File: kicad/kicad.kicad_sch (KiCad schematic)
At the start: 12 parts, among them K1 RP1A23D5, U1 WeMos_D1_mini, X1 250-202, X2 250-202, X3 250-203

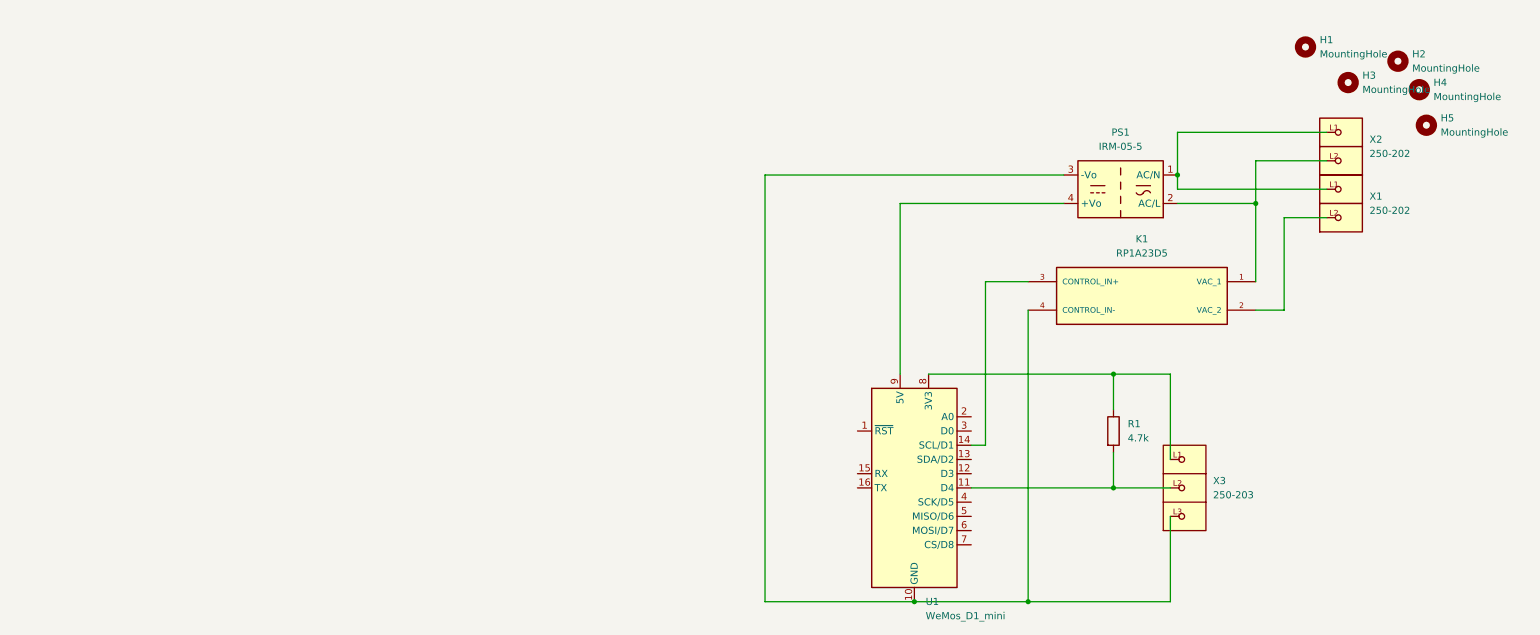
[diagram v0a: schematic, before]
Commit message: Small schematic & footprint cleanups
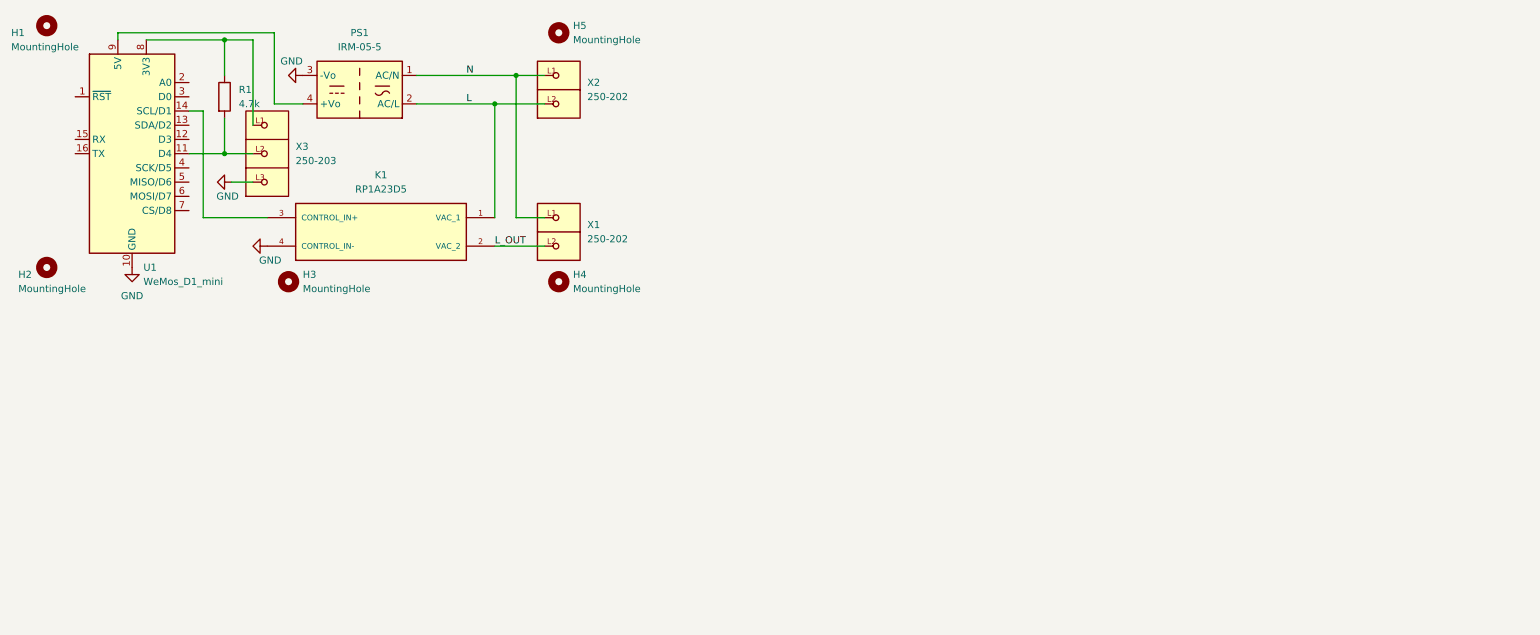
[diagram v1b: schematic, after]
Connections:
- net N: now reaches PS1.1 (AC/N), X1.L1, X2.L1
- net L: now reaches K1.1 (VAC_1), PS1.2 (AC/L), X2.L2
- net GND: now reaches K1.4 (CONTROL_IN-), PS1.3 (-Vo), U1.10 (GND), X3.L3
- net L_OUT: now reaches K1.2 (VAC_2), X1.L2
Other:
- moved on the sheet: H1, H2, H3, H4, H5, K1, PS1, R1, U1, X1, X2, X3

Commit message: WIP: some more schematic & footprint updates
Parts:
- H1, H2, H3, H4, H5: footprint MountingHole:MountingHole_2.5mm -> MountingHole:MountingHole_2.7mm_M2.5
- K1: footprint RELAY_RP1A23D5 -> snapeda-libraries:RELAY_RP1A23D5
- R1: footprint Resistor_THT:R_Axial_DIN0207_L6.3mm_D2.5mm_P7.62mm_Horizontal -> Resistor_THT:R_Axial_DIN0207_L6.3mm_D2.5mm_P10.16mm_Horizontal
- X1, X2: footprint P-250-202 -> snapeda-libraries:P-250-202
- X3: footprint P-250-203 -> snapeda-libraries:P-250-203
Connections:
- net 3V3: now reaches R1.1, U1.8 (3V3), X3.L1
- net DATA: now reaches R1.2, U1.11 (D4), X3.L2
- no-connect marks 0 -> 4
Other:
- moved on the sheet: H2, H3, H4, H5, K1, PS1, R1, X1, X2, X3
